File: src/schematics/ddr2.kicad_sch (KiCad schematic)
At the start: 23 parts, among them U11 IS43DR86400E

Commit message: Add remaining component footprints (#79)
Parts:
- C105, C106, C107, C108, C109, C110, C111, C112, C113, C114, C115, C116, C117, C118, C119, C120, C121, C122: footprint (none) -> Capacitor_SMD:C_0402_1005Metric
- R23, R24, R25, R26: footprint (none) -> Resistor_SMD:R_0603_1608Metric
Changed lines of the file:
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@@
 		(polyline
 			(pts
-				(xy 166.37 76.2) (xy 166.37 96.52) (xy 168.91 96.52) (xy 168.91 76.2)
+				(xy 166.37 120.65) (xy 166.37 105.41) (xy 168.91 105.41) (xy 168.91 120.65)
 			)
 			(stroke
@@
 		(polyline
 			(pts
-				(xy 118.11 118.11) (xy 118.11 123.19) (xy 120.65 123.19) (xy 120.65 118.11)
+				(xy 177.8 102.87) (xy 177.8 97.79) (xy 180.34 97.79) (xy 180.34 102.87)
 			)
 			(stroke
@@
 		(polyline
 			(pts
-				(xy 166.37 120.65) (xy 166.37 105.41) (xy 168.91 105.41) (xy 168.91 120.65)
+				(xy 130.81 73.66) (xy 130.81 115.57) (xy 133.35 115.57) (xy 133.35 73.66)
 			)
 			(stroke
@@
 		(polyline
 			(pts
-				(xy 130.81 73.66) (xy 130.81 115.57) (xy 133.35 115.57) (xy 133.35 73.66)
+				(xy 118.11 118.11) (xy 118.11 123.19) (xy 120.65 123.19) (xy 120.65 118.11)
 			)
 			(stroke
@@
 		(polyline
 			(pts
-				(xy 177.8 102.87) (xy 177.8 97.79) (xy 180.34 97.79) (xy 180.34 102.87)
+				(xy 166.37 76.2) (xy 166.37 96.52) (xy 168.91 96.52) (xy 168.91 76.2)
 			)
 			(stroke
@@
 			)
 		)
-		(property "Footprint" ""
+		(property "Footprint" "Capacitor_SMD:C_0402_1005Metric"
 			(at 85.09 35.56 0)
 			(effects
@@
 			)
 		)
-		(property "Footprint" ""
+		(property "Footprint" "Capacitor_SMD:C_0402_1005Metric"
 			(at 115.57 52.07 0)
 			(effects
@@
 			)
 		)
-		(property "Footprint" ""
+		(property "Footprint" "Capacitor_SMD:C_0402_1005Metric"
 			(at 115.57 35.56 0)
 			(effects
@@
 			)
 		)
-		(property "Footprint" ""
+		(property "Footprint" "Resistor_SMD:R_0603_1608Metric"
 			(at 129.54 132.08 0)
 			(effects
@@
 			)
 		)
-		(property "Footprint" ""
+		(property "Footprint" "Capacitor_SMD:C_0402_1005Metric"
 			(at 85.09 52.07 0)
 			(effects
@@
 			)
 		)
-		(property "Footprint" ""
+		(property "Footprint" "Capacitor_SMD:C_0402_1005Metric"
 			(at 138.43 35.56 0)
 			(effects
@@
 			)
 		)
-		(property "Footprint" ""
+		(property "Footprint" "Capacitor_SMD:C_0402_1005Metric"
 			(at 138.43 52.07 0)
 			(effects
@@
 			)
 		)
-		(property "Footprint" ""
+		(property "Footprint" "Capacitor_SMD:C_0402_1005Metric"
 			(at 163.83 52.07 0)
 			(effects
@@
 			)
 		)
-		(property "Footprint" ""
+		(property "Footprint" "Resistor_SMD:R_0603_1608Metric"
 			(at 222.25 67.31 0)
 			(effects
@@
 			)
 		)
-		(property "Footprint" ""
+		(property "Footprint" "Capacitor_SMD:C_0402_1005Metric"
 			(at 95.25 35.56 0)
 			(effects
@@
 			)
 		)
-		(property "Footprint" ""
+		(property "Footprint" "Capacitor_SMD:C_0402_1005Metric"
 			(at 176.53 52.07 0)
 			(effects
@@
 			)
 		)
-		(property "Footprint" ""
+		(property "Footprint" "Capacitor_SMD:C_0402_1005Metric"
 			(at 95.25 52.07 0)
 			(effects
@@
 			)
 		)
-		(property "Footprint" ""
+		(property "Footprint" "Capacitor_SMD:C_0402_1005Metric"
 			(at 203.2 77.47 0)
 			(effects
@@
 			)
 		)
-		(property "Footprint" ""
+		(property "Footprint" "Capacitor_SMD:C_0402_1005Metric"
 			(at 74.93 52.07 0)
 			(effects
@@
 			)
 		)
-		(property "Footprint" ""
+		(property "Footprint" "Capacitor_SMD:C_0402_1005Metric"
 			(at 105.41 52.07 0)
 			(effects
@@
 			)
 		)
-		(property "Footprint" ""
+		(property "Footprint" "Resistor_SMD:R_0603_1608Metric"
 			(at 124.46 132.08 0)
 			(effects
@@
 			)
 		)
-		(property "Footprint" ""
+		(property "Footprint" "Capacitor_SMD:C_0402_1005Metric"
 			(at 128.27 35.56 0)
 			(effects
@@
 			)
 		)
-		(property "Footprint" ""
+		(property "Footprint" "Capacitor_SMD:C_0402_1005Metric"
 			(at 212.09 77.47 0)
 			(effects
@@
 			)
 		)
-		(property "Footprint" ""
+		(property "Footprint" "Capacitor_SMD:C_0402_1005Metric"
 			(at 128.27 52.07 0)
 			(effects
@@
 			)
 		)
-		(property "Footprint" ""
+		(property "Footprint" "Capacitor_SMD:C_0402_1005Metric"
 			(at 105.41 35.56 0)
 			(effects
@@
 			)
 		)
-		(property "Footprint" ""
+		(property "Footprint" "Capacitor_SMD:C_0402_1005Metric"
 			(at 127 139.7 0)
 			(effects
@@
 			)
 		)
-		(property "Footprint" ""
+		(property "Footprint" "Resistor_SMD:R_0603_1608Metric"
 			(at 222.25 77.47 0)
 			(effects

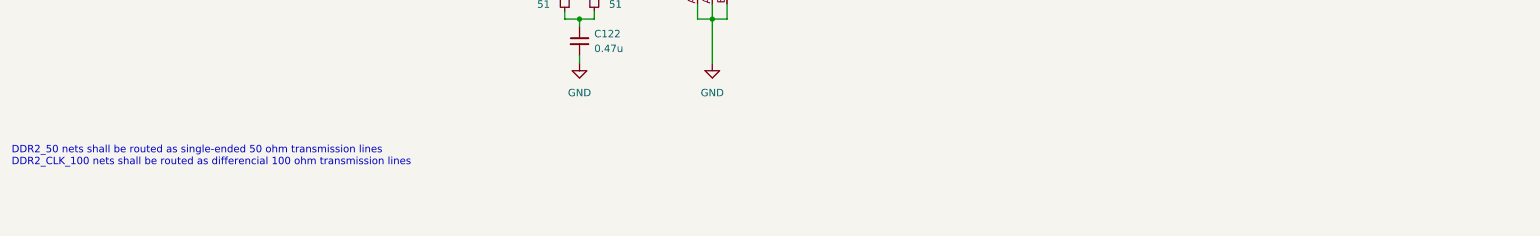
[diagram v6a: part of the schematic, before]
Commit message: Add notes on the schematic
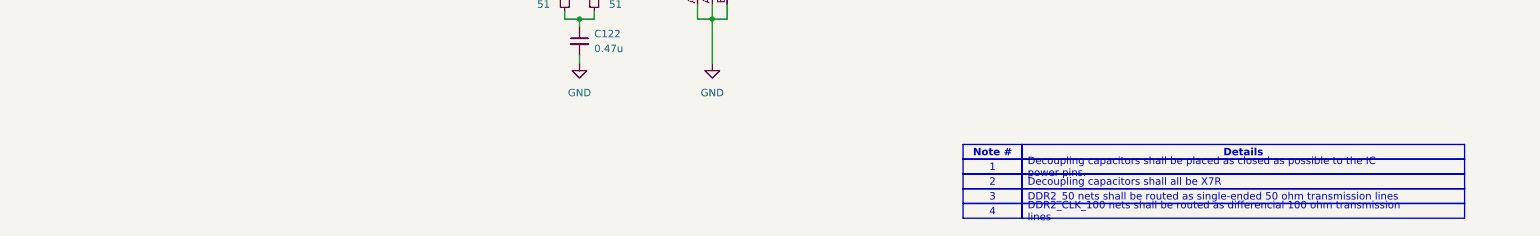
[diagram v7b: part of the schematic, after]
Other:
- note removed: "DDR2_50 nets shall be routed as single-ended 50 ohm transmission lines DDR2_CLK_100 nets shall be routed as differencial 100 ohm transmission lines"
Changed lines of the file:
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@@
 		(comment 3 "${Part Number}")
 	)
-	(text "DDR2_50 nets shall be routed as single-ended 50 ohm transmission lines\nDDR2_CLK_100 nets shall be routed as differencial 100 ohm transmission lines"
+	(text_box "Decoupling capacitors shall be placed as closed as possible to the IC power pins."
 		(exclude_from_sim no)
-		(at 29.21 159.512 0)
-		(effects
-			(font
-				(size 1.27 1.27)
+		(at 203.2 160.02 0)
+		(size 76.2 2.54)
+		(margins 0.9525 0.9525 0.9525 0.9525)
+		(stroke
+			(width 0)
+			(type solid)
+			(color 0 0 0 1)
+		)
+		(fill
+			(type none)
+		)
+		(effects
+			(font
+				(face "Arial")
+				(size 1.27 1.27)
+				(color 0 0 0 1)
 			)
 			(justify left)
+		)
+	)
+	(text_box "DDR2_50 nets shall be routed as single-ended 50 ohm transmission lines"
+		(exclude_from_sim no)
+		(at 203.2 165.1 0)
+		(size 76.2 2.54)
+		(margins 0.9525 0.9525 0.9525 0.9525)
+		(stroke
+			(width 0)
+			(type solid)
+			(color 0 0 0 1)
+		)
+		(fill
+			(type none)
+		)
+		(effects
+			(font
+				(face "Arial")
+				(size 1.27 1.27)
+				(color 0 0 0 1)
+			)
+			(justify left)
+		)
+	)
+	(text_box "Note #"
+		(exclude_from_sim no)
+		(at 193.04 157.48 0)
+		(size 10.16 2.54)
+		(margins 0.9525 0.9525 0.9525 0.9525)
+		(stroke
+			(width 0)
+			(type solid)
+			(color 0 0 0 1)
+		)
+		(fill
+			(type none)
+		)
+		(effects
+			(font
+				(face "Arial")
+				(size 1.27 1.27)
+				(bold yes)
+				(color 0 0 0 1)
+			)
+		)
+	)
+	(text_box "2"
+		(exclude_from_sim no)
+		(at 193.04 162.56 0)
+		(size 10.16 2.54)
+		(margins 0.9525 0.9525 0.9525 0.9525)
+		(stroke
+			(width 0)
+			(type solid)
+			(color 0 0 0 1)
+		)
+		(fill
+			(type none)
+		)
+		(effects
+			(font
+				(face "Arial")
+				(size 1.27 1.27)
+				(color 0 0 0 1)
+			)
+		)
+	)
+	(text_box "3"
+		(exclude_from_sim no)
+		(at 193.04 165.1 0)
+		(size 10.16 2.54)
+		(margins 0.9525 0.9525 0.9525 0.9525)
+		(stroke
+			(width 0)
+			(type solid)
+			(color 0 0 0 1)
+		)
+		(fill
+			(type none)
+		)
+		(effects
+			(font
+				(face "Arial")
+				(size 1.27 1.27)
+				(color 0 0 0 1)
+			)
+		)
+	)
+	(text_box "4"
+		(exclude_from_sim no)
+		(at 193.04 167.64 0)
+		(size 10.16 2.54)
+		(margins 0.9525 0.9525 0.9525 0.9525)
+		(stroke
+			(width 0)
+			(type solid)
+			(color 0 0 0 1)
+		)
+		(fill
+			(type none)
+		)
+		(effects
+			(font
+				(face "Arial")
+				(size 1.27 1.27)
+				(color 0 0 0 1)
+			)
+		)
+	)
+	(text_box "Details"
+		(exclude_from_sim no)
+		(at 203.2 157.48 0)
+		(size 76.2 2.54)
+		(margins 0.9525 0.9525 0.9525 0.9525)
+		(stroke
+			(width 0)
+			(type solid)
+			(color 0 0 0 1)
+		)
+		(fill
+			(type none)
+		)
+		(effects
+			(font
+				(face "Arial")
+				(size 1.27 1.27)
+				(bold yes)
+				(color 0 0 0 1)
+			)
+		)
+	)
+	(text_box "DDR2_CLK_100 nets shall be routed as differencial 100 ohm transmission lines"
+		(exclude_from_sim no)
+		(at 203.2 167.64 0)
+		(size 76.2 2.54)
+		(margins 0.9525 0.9525 0.9525 0.9525)
+		(stroke
+			(width 0)
+			(type solid)
+			(color 0 0 0 1)
+		)
+		(fill
+			(type none)
+		)
+		(effects
+			(font
+				(face "Arial")
+				(size 1.27 1.27)
+				(color 0 0 0 1)
+			)
+			(justify left)
+		)
+	)
+	(text_box "Decoupling capacitors shall all be X7R"
+		(exclude_from_sim no)
+		(at 203.2 162.56 0)
+		(size 76.2 2.54)
+		(margins 0.9525 0.9525 0.9525 0.9525)
+		(stroke
+			(width 0)
+			(type solid)
+			(color 0 0 0 1)
+		)
+		(fill
+			(type none)
+		)
+		(effects
+			(font
+				(face "Arial")
+				(size 1.27 1.27)
+				(color 0 0 0 1)
+			)
+			(justify left)
+		)
+	)
+	(text_box "1"
+		(exclude_from_sim no)
+		(at 193.04 160.02 0)
+		(size 10.16 2.54)
+		(margins 0.9525 0.9525 0.9525 0.9525)
+		(stroke
+			(width 0)
+			(type solid)
+			(color 0 0 0 1)
+		)
+		(fill
+			(type none)
+		)
+		(effects
+			(font
+				(face "Arial")
+				(size 1.27 1.27)
+				(color 0 0 0 1)
+			)
 		)
 	)
@@
 		(polyline
 			(pts
-				(xy 166.37 76.2) (xy 166.37 96.52) (xy 168.91 96.52) (xy 168.91 76.2)
+				(xy 130.81 73.66) (xy 130.81 115.57) (xy 133.35 115.57) (xy 133.35 73.66)
 			)
 			(stroke
@@
 		(polyline
 			(pts
-				(xy 130.81 73.66) (xy 130.81 115.57) (xy 133.35 115.57) (xy 133.35 73.66)
+				(xy 166.37 120.65) (xy 166.37 105.41) (xy 168.91 105.41) (xy 168.91 120.65)
 			)
 			(stroke
@@
 		(polyline
 			(pts
-				(xy 177.8 102.87) (xy 177.8 97.79) (xy 180.34 97.79) (xy 180.34 102.87)
+				(xy 166.37 76.2) (xy 166.37 96.52) (xy 168.91 96.52) (xy 168.91 76.2)
 			)
 			(stroke
@@
 		(polyline
 			(pts
-				(xy 166.37 120.65) (xy 166.37 105.41) (xy 168.91 105.41) (xy 168.91 120.65)
+				(xy 177.8 102.87) (xy 177.8 97.79) (xy 180.34 97.79) (xy 180.34 102.87)
 			)
 			(stroke
